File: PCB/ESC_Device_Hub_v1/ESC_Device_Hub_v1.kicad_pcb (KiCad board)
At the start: 4 copper layers, 50 x 90 mm, 134 parts, among them J1 Conn_01x04, J10 Conn_01x06, J11 Conn_01x02, J12 Conn_01x02, J13 Conn_01x02, J14 Conn_01x02, J15 Conn_01x02, J16 Conn_01x02, J17 Conn_01x02, J18 Conn_01x02, J2 Conn_01x04, J20 Conn_01x01, J21 Conn_01x01, J22 Conn_01x02, J23 Conn_01x04, J3 Conn_01x04, J4 Conn_01x04, J5 Conn_01x04, J6 Conn_01x04, J7 Conn_01x06, J8 Conn_01x06, J9 Conn_01x06, SW1 SW_Push, SW2 SW_Push, SW4 SW_DIP_x02, U1 ISO1042BQDWVQ1, U10 LM66100DCK, U11 LM66100DCK, U18 USB_Type-C, U2 MCP2562FD-H/MF, U3 IS25LP064D-JLLE, U4 STM32H563RGVx, U6 TLP293, U7 NJM2884U1-33, U8 RFM-0505S, Y1 FC2012SN 32.768K-70NNA0KC0, Y2 XRCGB25M000FFS1AR0

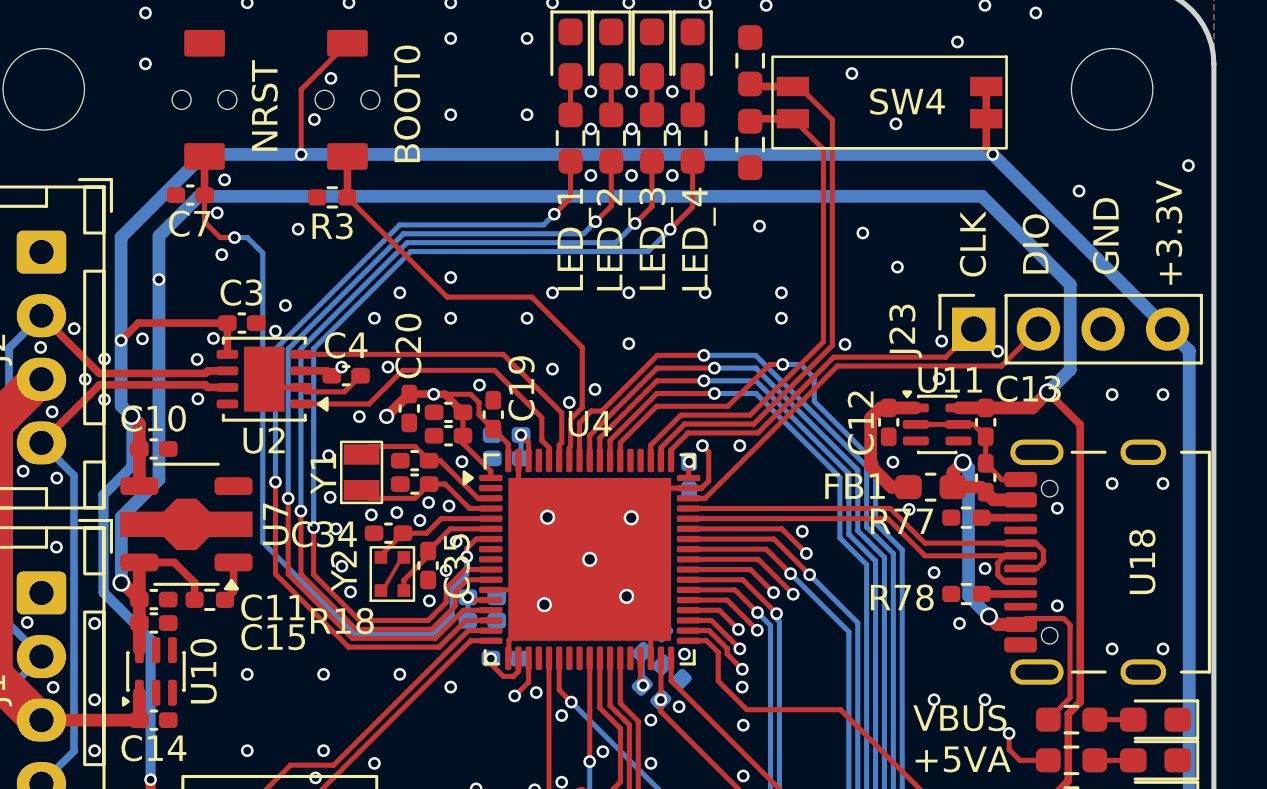
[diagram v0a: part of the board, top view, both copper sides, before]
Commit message: PIの追加　基板PCB変更
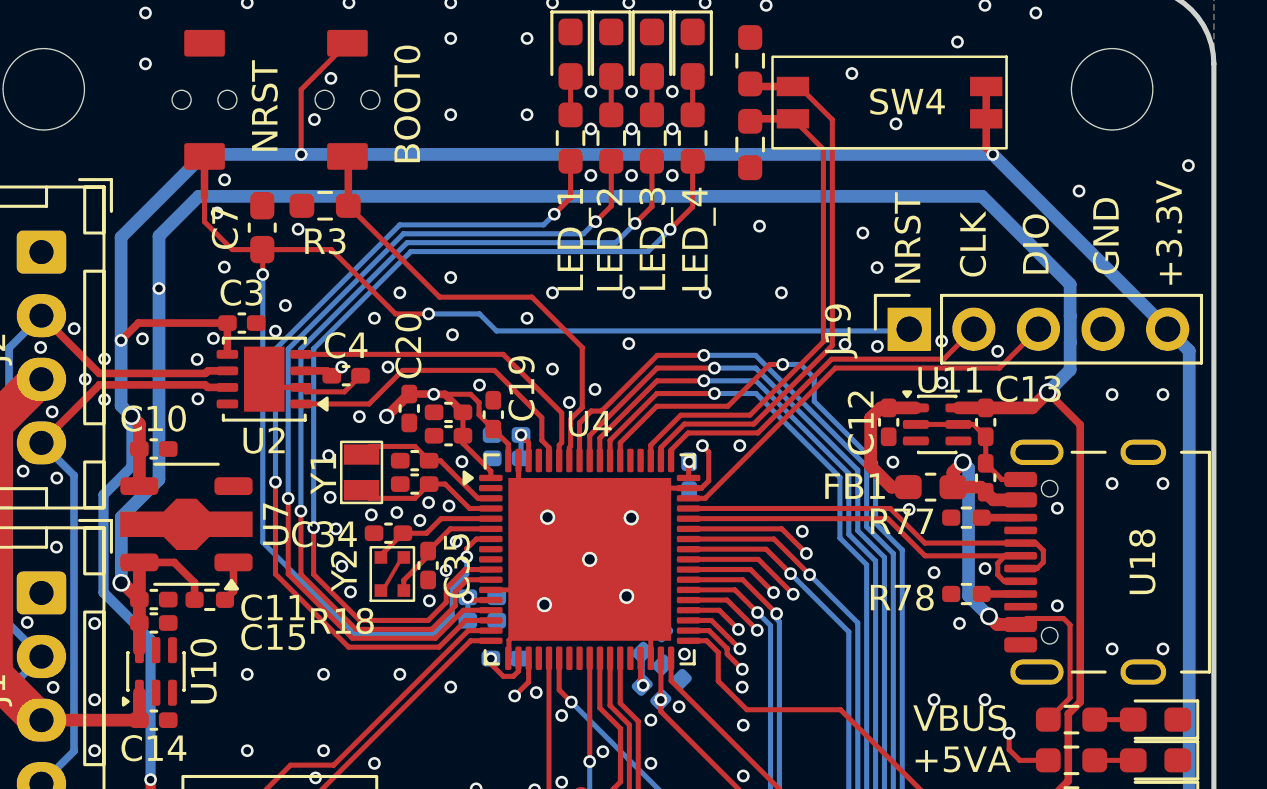
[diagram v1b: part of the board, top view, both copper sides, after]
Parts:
- removed J23: Conn_01x04, Connector_PinSocket_2.54mm:PinSocket_1x04_P2.54mm_Vertical
- added J19: Conn_01x05, Connector_PinSocket_2.54mm:PinSocket_1x05_P2.54mm_Vertical, F.Cu at (178.0, 43.4)
- C7: footprint Capacitor_SMD:C_0402_1005Metric_Pad0.74x0.62mm_HandSolder -> Capacitor_SMD:C_0603_1608Metric_Pad1.08x0.95mm_HandSolder
- R3: footprint Resistor_SMD:R_0402_1005Metric_Pad0.72x0.64mm_HandSolder -> Resistor_SMD:R_0603_1608Metric_Pad0.98x0.95mm_HandSolder
- moved C7 3.11 mm to (152.6, 39.4), turned to 90 degrees
- moved R3 0.43 mm to (155.1, 38.6)
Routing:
- net NRST: track 29.9 -> 56.8 mm, vias 2 -> 3
